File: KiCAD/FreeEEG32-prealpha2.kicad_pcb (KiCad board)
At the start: 2 copper layers, 99.1 x 99.1 mm, 205 parts, among them J1 Conn_02x08_Odd_Even, J10 Conn_02x08_Odd_Even, J11 Conn_02x08_Odd_Even, J12 Conn_02x08_Odd_Even, J13 Conn_02x08_Odd_Even, J14 Conn_02x08_Odd_Even, J15 Conn_02x08_Odd_Even, J16 Conn_02x08_Odd_Even, J17 Conn_01x03, J18 Conn_01x03, J19 Conn_01x03, J2 Conn_02x08_Odd_Even, J20 Conn_01x03, J21 Conn_01x04, J22 Conn_01x04, J23 Conn_01x02, J24 Conn_01x02, J25 Conn_02x18_Odd_Even, J26 Conn_02x18_Odd_Even, J27 Conn_02x18_Odd_Even, J28 Conn_02x18_Odd_Even, J29 Conn_01x03, J3 Conn_02x08_Odd_Even, J30 Conn_01x03, J31 Conn_01x04, J32 Conn_01x03, J33 Conn_01x03, J34 Conn_01x04, J35 Conn_01x02, J36 Conn_01x02, J37 Conn_01x05, J38 Conn_01x04, J39 Conn_02x04_Odd_Even, J4 Conn_02x08_Odd_Even, J40 Conn_02x04_Odd_Even, J41 Conn_02x04_Odd_Even, J42 Conn_02x04_Odd_Even, J43 Conn_02x04_Odd_Even, J44 Conn_02x04_Odd_Even, J5 Conn_02x08_Odd_Even, J6 Conn_02x08_Odd_Even, J7 Conn_02x08_Odd_Even, J8 Conn_02x08_Odd_Even, J9 Conn_02x08_Odd_Even, T1 da2303, U1 AD7779, U10 LP5907, U11 LSM6DS3, U12 SN6505A, U13 473521001, U14 ISO7341c, U15 ISO7341c, U16 ISO7341c, U2 AD7779, U3 AD7779, U4 AD7779, U5 LP5907, U6 LP5907, U7 ADR4525, U8 FXO-SM7_OSC-SMD7050_short, U9 STM32F765ZITx

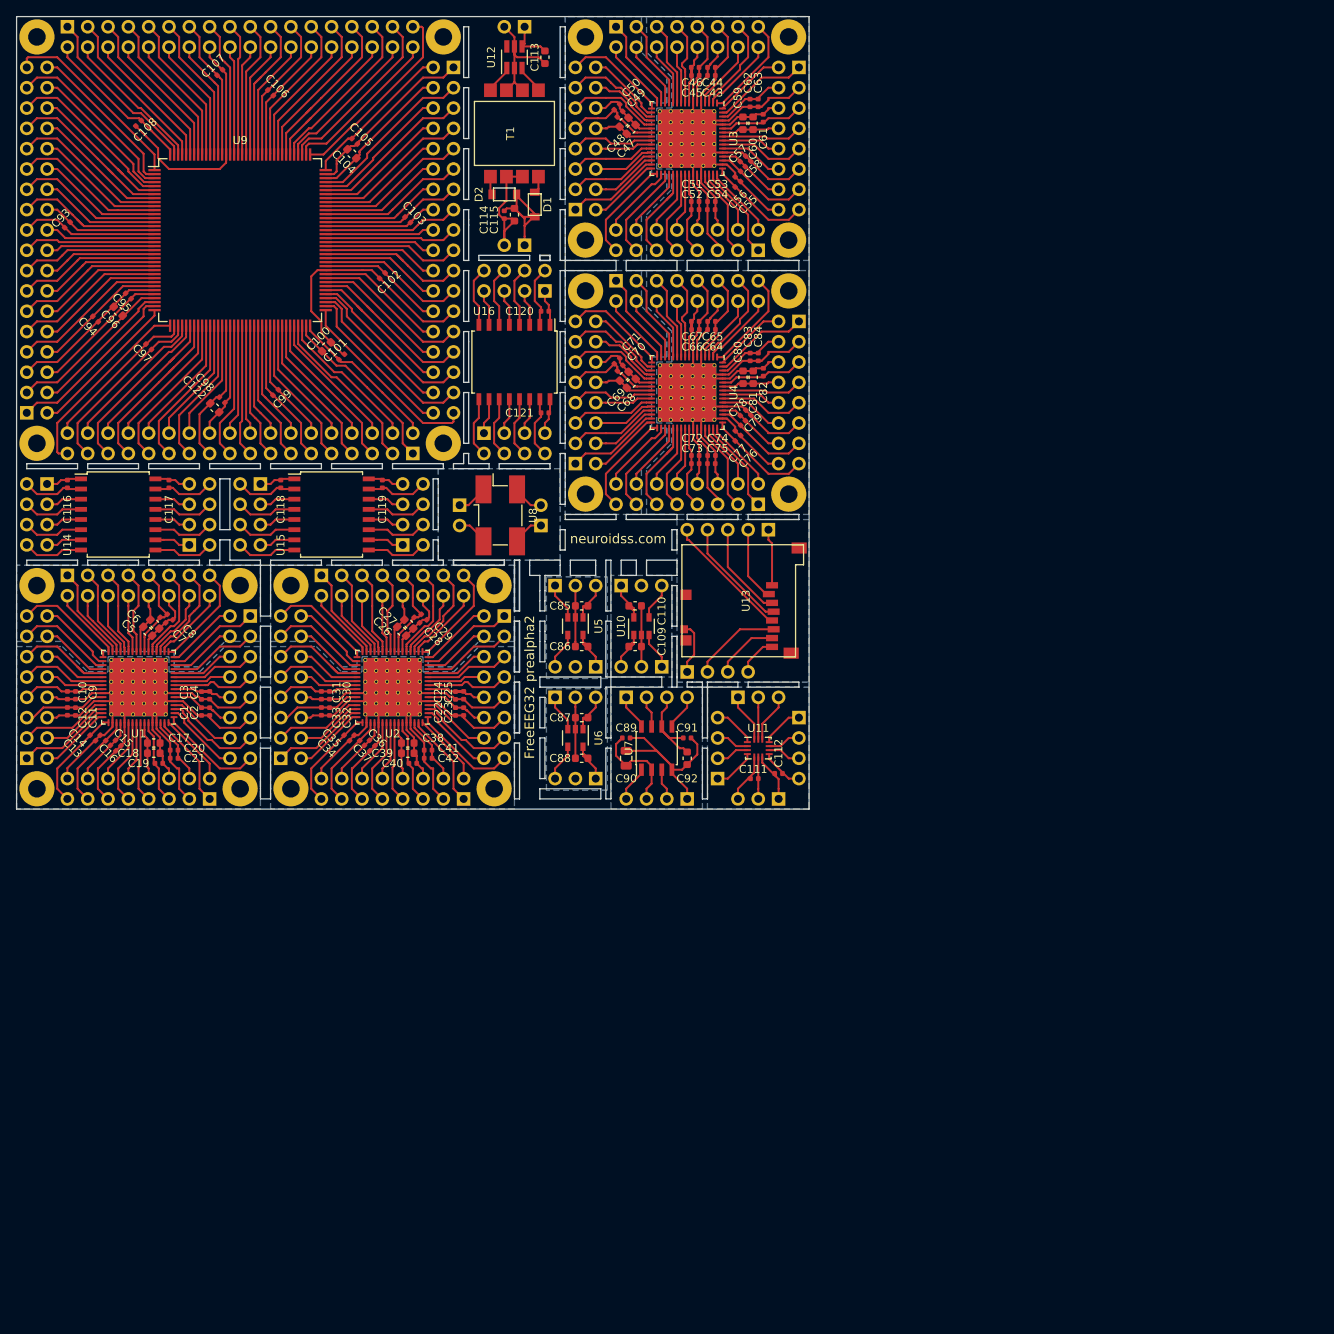
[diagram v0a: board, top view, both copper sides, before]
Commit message: added usb, crystals
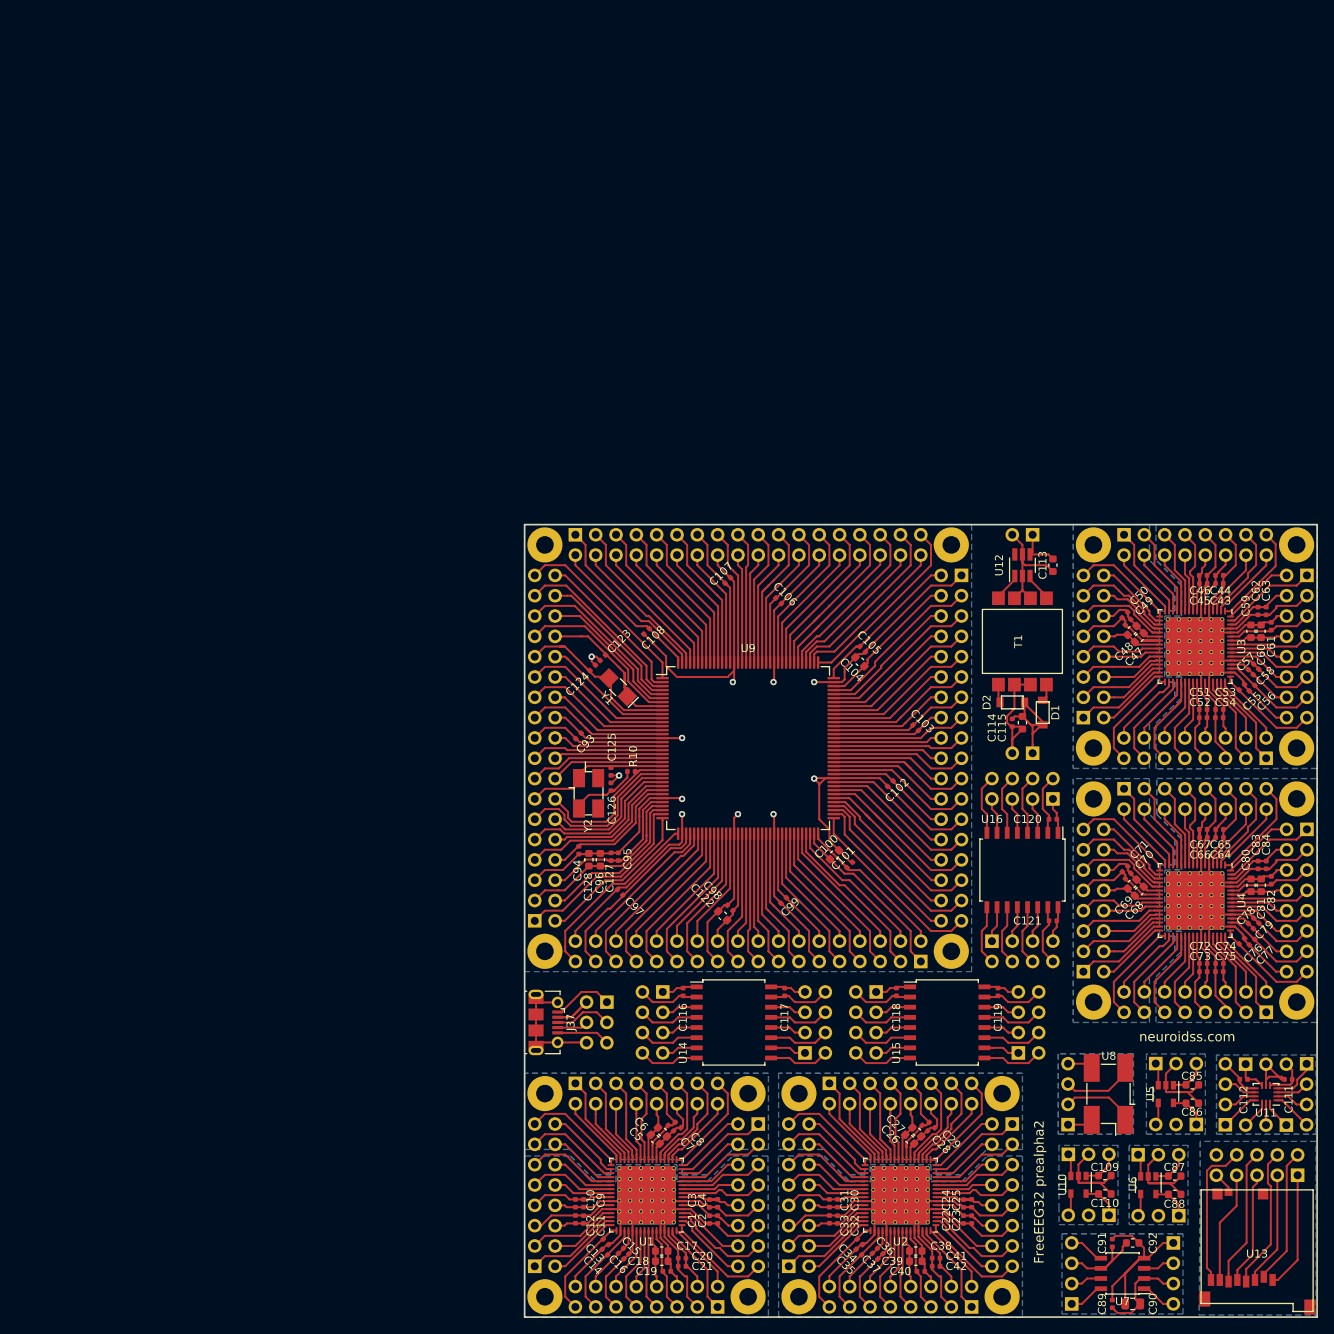
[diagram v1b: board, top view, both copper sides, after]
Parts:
- added C123: CL1, Capacitor_SMD:C_0402_1005Metric, F.Cu at (23.7, 30.6)
- added C124: CL2, Capacitor_SMD:C_0402_1005Metric, F.Cu at (22.5, 31.9)
- added C125: CL1, Capacitor_SMD:C_0402_1005Metric, F.Cu at (24.8, 44.8)
- added C126: CL2, Capacitor_SMD:C_0402_1005Metric, F.Cu at (24.8, 46.7)
- added C127: 1u, Capacitor_SMD:C_0402_1005Metric, F.Cu at (24.8, 55.5)
- added C128: 1u, Capacitor_SMD:C_0603_1608Metric, F.Cu at (22.0, 55.9)
- added R10: R_EXT, Resistor_SMD:R_0402_1005Metric, F.Cu at (27.3, 44.8)
- added Y1: 32768Hz, Crystal:Crystal_SMD_EuroQuartz_EQ161-2Pin_3.2x1.5mm_HandSoldering, F.Cu at (25.7, 34.3)
- added Y2: 8MHz, smd5032:Crystal_SMD_EuroQuartz_MJ-4Pin_5.0x3.2mm_HandSoldering, F.Cu at (22.0, 47.6)
- J23: value Conn_01x02 -> Conn_01x04; footprint Connector_PinHeader_2.54mm:PinHeader_1x02_P2.54mm_Vertical -> Connector_PinHeader_2.54mm:PinHeader_1x04_P2.54mm_Vertical
- J24: value Conn_01x02 -> Conn_02x05_Odd_Even; footprint Connector_PinHeader_2.54mm:PinHeader_1x02_P2.54mm_Vertical -> Connector_PinHeader_2.54mm:PinHeader_2x05_P2.54mm_Vertical
- J37: value Conn_01x05 -> USB_B_Micro; footprint Connector_PinHeader_2.54mm:PinHeader_1x05_P2.54mm_Vertical -> Connector_USB:USB_Micro-B_Molex-105017-0001; moved to F.Cu
- J38: value Conn_01x04 -> Conn_02x03_Odd_Even; footprint Connector_PinHeader_2.54mm:PinHeader_1x04_P2.54mm_Vertical -> Connector_PinHeader_2.54mm:PinHeader_2x03_P2.54mm_Vertical
- REF** (x20): value MountingHole_2.2mm_M2_Pad -> MH_2.2mm_M2
- moved J24 134.1 mm to (110.6, 95.3), turned to 90 degrees
- moved U8 104.9 mm to (87.0, 85.1), turned to 90 degrees
- moved U13 103.5 mm to (105.5, 104.1), turned to 0 degrees
- moved C117 99.8 mm to (46.5, 72.4)
- moved C118 99.8 mm to (60.5, 72.4)
- moved C119 99.8 mm to (73.2, 72.4)
- moved J39 99.8 mm to (31.2, 72.4)
- moved J40 99.8 mm to (49.0, 80.0)
- moved J41 99.8 mm to (57.9, 72.4)
- moved U15 99.8 mm to (66.8, 76.2)
- moved C116 99.8 mm to (33.8, 72.4)
- moved J42 99.8 mm to (75.7, 80.0)
- moved U14 99.8 mm to (40.1, 76.2)
- moved J23 99.8 mm to (81.9, 89.0)
- moved J30 99.6 mm to (87.0, 100.3), turned to 90 degrees
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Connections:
- net /ACCEL&GYRO/1 renamed /ACCEL&GYRO/1_SDO/SA0
- net /ACCEL&GYRO/10 renamed /ACCEL&GYRO/10_NC
- net /ACCEL&GYRO/11 renamed /ACCEL&GYRO/11_NC
- net /ACCEL&GYRO/12 renamed /ACCEL&GYRO/12_CS
- net /ACCEL&GYRO/13 renamed /ACCEL&GYRO/13_SCL
- net /ACCEL&GYRO/14 renamed /ACCEL&GYRO/14_SDA
- net /ACCEL&GYRO/2 renamed /ACCEL&GYRO/2_SDx
- net /ACCEL&GYRO/3 renamed /ACCEL&GYRO/3_SCx
- net /ACCEL&GYRO/4 renamed /ACCEL&GYRO/4_INT1
- net /ACCEL&GYRO/5 renamed /ACCEL&GYRO/5_VDDIO
- net /ACCEL&GYRO/6 renamed /ACCEL&GYRO/6_GND
- net /ACCEL&GYRO/7 renamed /ACCEL&GYRO/7_GND
- net /ACCEL&GYRO/8 renamed /ACCEL&GYRO/8_VDD
- net /ACCEL&GYRO/9 renamed /ACCEL&GYRO/9_INT2
- net /ADC1/1 renamed /ADC1/1_AIN0-
- net /ADC1/10 renamed /ADC1/10_AIN2+
- net /ADC1/11 renamed /ADC1/11_AIN3-
- net /ADC1/12 renamed /ADC1/12_AIN3+
- net /ADC1/13 renamed /ADC1/13_MODE0_GPIO0
- net /ADC1/14 renamed /ADC1/14_MODE1_GPIO1
- net /ADC1/15 renamed /ADC1/15_MODE2_GPIO2
- net /ADC1/16 renamed /ADC1/16_MODE3_ALERT
- net /ADC1/17 renamed /ADC1_17_CONVST_SAR
- net /ADC1/18 renamed /ADC1_18_ALERT_CS
- net /ADC1/19 renamed /ADC1_19_DCLK2_SCLK
- net /ADC1/2 renamed /ADC1/2_AIN0+
- net /ADC1/20 renamed /ADC1_20_DCLK1_SDI
- net /ADC1/21 renamed /ADC1_21_DCLK0_SDO
- net /ADC1/23 renamed /ADC1_23_DREGCAP
- net /ADC1/24 renamed /ADC1_24_IOVDD
- net /ADC1/25 renamed /ADC1_25_DOUT3
- net /ADC1/26 renamed /ADC1_26_DOUT2
- net /ADC1/27 renamed /ADC1_27_DOUT1
- net /ADC1/28 renamed /ADC1_28_DOUT0
- net /ADC1/29 renamed /ADC1_29_DCLK
- net /ADC1/3 renamed /ADC1/3_AIN1-
- net /ADC1/30 renamed /ADC1_30_DRDY
- net /ADC1/31 renamed /ADC1_31_XTAL1
- net /ADC1/32 renamed /ADC1_32_XTAL2_MCLK
- net /ADC1/33 renamed /ADC1_33_START
- net /ADC1/34 renamed /ADC1_34_SYNC_OUT
- net /ADC1/35 renamed /ADC1_35_SYNC_IN
- net /ADC1/36 renamed /ADC1_36_RESET
- net /ADC1/37 renamed /ADC1/37_AIN7+
- net /ADC1/38 renamed /ADC1/38_AIN7-
- net /ADC1/39 renamed /ADC1/39_AIN6+
- net /ADC1/4 renamed /ADC1/4_AIN1+
- net /ADC1/40 renamed /ADC1/40_AIN6-
- net /ADC1/41 renamed /ADC1_41_REF2+
- net /ADC1/43 renamed /ADC1_43_AVDD1B
- net /ADC1/45 renamed /ADC1/45_AIN5+
- net /ADC1/46 renamed /ADC1/46_AIN5-
- net /ADC1/47 renamed /ADC1/47_AIN4+
- net /ADC1/48 renamed /ADC1/48_AIN4-
- net /ADC1/49 renamed /ADC1/49_REF_OUT
- net /ADC1/51 renamed /ADC1/51_AREG2CAP
- net /ADC1/52 renamed /ADC1_52_AVDD2B
- net /ADC1/54 renamed /ADC1_54_FORMAT1
- net /ADC1/55 renamed /ADC1_55_FORMAT0
- net /ADC1/56 renamed /ADC1_56_CLK_SEL
- net /ADC1/57 renamed /ADC1/57_VCM
- net /ADC1/58 renamed /ADC1_58_AVDD2A
- net /ADC1/59 renamed /ADC1/59_AREG1CAP
- net /ADC1/6 renamed /ADC1_6_AVDD1A
- net /ADC1/62 renamed /ADC1_62_AVDD4
- net /ADC1/63 renamed /ADC1/63_AUXAIN+
- net /ADC1/64 renamed /ADC1/64_AUXAIN-
- net /ADC1/8 renamed /ADC1_8_REF1+
- net /ADC1/9 renamed /ADC1/9_AIN2-
- net /ADC2/1 renamed /ADC2/1_AIN0-
- net /ADC2/10 renamed /ADC2/10_AIN2+
- net /ADC2/11 renamed /ADC2/11_AIN3-
- net /ADC2/12 renamed /ADC2/12_AIN3+
- net /ADC2/13 renamed /ADC2/13_MODE0_GPIO0
- net /ADC2/14 renamed /ADC2/14_MODE1_GPIO1
- net /ADC2/15 renamed /ADC2/15_MODE2_GPIO2
- net /ADC2/16 renamed /ADC2/16_MODE3_ALERT
- net /ADC2/17 renamed /ADC2_17_CONVST_SAR
- net /ADC2/18 renamed /ADC2_18_ALERT_CS
- net /ADC2/19 renamed /ADC2_19_DCLK2_SCLK
- net /ADC2/2 renamed /ADC2/2_AIN0+
- net /ADC2/20 renamed /ADC2_20_DCLK1_SDI
- net /ADC2/21 renamed /ADC2_21_DCLK0_SDO
- net /ADC2/23 renamed /ADC2_23_DREGCAP
- net /ADC2/24 renamed /ADC2_24_IOVDD
- net /ADC2/25 renamed /ADC2_25_DOUT3
- net /ADC2/26 renamed /ADC2_26_DOUT2
- net /ADC2/27 renamed /ADC2_27_DOUT1
- net /ADC2/28 renamed /ADC2_28_DOUT0
- net /ADC2/29 renamed /ADC2_29_DCLK
- net /ADC2/3 renamed /ADC2/3_AIN1-
- net /ADC2/30 renamed /ADC2_30_DRDY
- net /ADC2/31 renamed /ADC2_31_XTAL1
- net /ADC2/32 renamed /ADC2_32_XTAL2_MCLK
- net /ADC2/33 renamed /ADC2_33_START
- net /ADC2/34 renamed /ADC2_34_SYNC_OUT
- net /ADC2/35 renamed /ADC2_35_SYNC_IN
- net /ADC2/36 renamed /ADC2_36_RESET
- net /ADC2/37 renamed /ADC2/37_AIN7+
- net /ADC2/38 renamed /ADC2/38_AIN7-
- net /ADC2/39 renamed /ADC2/39_AIN6+
- net /ADC2/4 renamed /ADC2/4_AIN1+
- net /ADC2/40 renamed /ADC2/40_AIN6-
- net /ADC2/41 renamed /ADC2_41_REF2+
- net /ADC2/43 renamed /ADC2_43_AVDD1B
- net /ADC2/45 renamed /ADC2/45_AIN5+
- net /ADC2/46 renamed /ADC2/46_AIN5-
- net /ADC2/47 renamed /ADC2/47_AIN4+
- net /ADC2/48 renamed /ADC2/48_AIN4-
- net /ADC2/49 renamed /ADC2/49_REF_OUT
- net /ADC2/51 renamed /ADC2/51_AREG2CAP
- net /ADC2/52 renamed /ADC2_52_AVDD2B
- net /ADC2/54 renamed /ADC2_54_FORMAT1
- net /ADC2/55 renamed /ADC2_55_FORMAT0
- net /ADC2/56 renamed /ADC2_56_CLK_SEL
- net /ADC2/57 renamed /ADC2/57_VCM
- net /ADC2/58 renamed /ADC2_58_AVDD2A
- net /ADC2/59 renamed /ADC2/59_AREG1CAP
- net /ADC2/6 renamed /ADC2_6_AVDD1A
- net /ADC2/62 renamed /ADC2_62_AVDD4
- net /ADC2/63 renamed /ADC2/63_AUXAIN+
- net /ADC2/64 renamed /ADC2/64_AUXAIN-
- net /ADC2/8 renamed /ADC2_8_REF1+
- net /ADC2/9 renamed /ADC2/9_AIN2-
- net /ADC3/1 renamed /ADC3/1_AIN0-
- net /ADC3/10 renamed /ADC3/10_AIN2+
- net /ADC3/11 renamed /ADC3/11_AIN3-
- net /ADC3/12 renamed /ADC3/12_AIN3+
- net /ADC3/13 renamed /ADC3/13_MODE0_GPIO0
- net /ADC3/14 renamed /ADC3/14_MODE1_GPIO1
- net /ADC3/15 renamed /ADC3/15_MODE2_GPIO2
- net /ADC3/16 renamed /ADC3/16_MODE3_ALERT
- net /ADC3/17 renamed /ADC3_17_CONVST_SAR
- net /ADC3/18 renamed /ADC3_18_ALERT_CS
- net /ADC3/19 renamed /ADC3_19_DCLK2_SCLK
- net /ADC3/2 renamed /ADC3/2_AIN0+
- net /ADC3/20 renamed /ADC3_20_DCLK1_SDI
- net /ADC3/21 renamed /ADC3_21_DCLK0_SDO
- net /ADC3/23 renamed /ADC3_23_DREGCAP
- net /ADC3/24 renamed /ADC3_24_IOVDD
- net /ADC3/25 renamed /ADC3_25_DOUT3
- net /ADC3/26 renamed /ADC3_26_DOUT2
- net /ADC3/27 renamed /ADC3_27_DOUT1
- net /ADC3/28 renamed /ADC3_28_DOUT0
- net /ADC3/29 renamed /ADC3_29_DCLK
- net /ADC3/3 renamed /ADC3/3_AIN1-
- net /ADC3/30 renamed /ADC3_30_DRDY
- net /ADC3/31 renamed /ADC3_31_XTAL1
- net /ADC3/32 renamed /ADC3_32_XTAL2_MCLK
- net /ADC3/33 renamed /ADC3_33_START
- net /ADC3/34 renamed /ADC3_34_SYNC_OUT
- net /ADC3/35 renamed /ADC3_35_SYNC_IN
- net /ADC3/36 renamed /ADC3_36_RESET
- net /ADC3/37 renamed /ADC3/37_AIN7+
- net /ADC3/38 renamed /ADC3/38_AIN7-
- net /ADC3/39 renamed /ADC3/39_AIN6+
- net /ADC3/4 renamed /ADC3/4_AIN1+
- net /ADC3/40 renamed /ADC3/40_AIN6-
- net /ADC3/41 renamed /ADC3_41_REF2+
- net /ADC3/43 renamed /ADC3_43_AVDD1B
- net /ADC3/45 renamed /ADC3/45_AIN5+
- net /ADC3/46 renamed /ADC3/46_AIN5-
- net /ADC3/47 renamed /ADC3/47_AIN4+
- net /ADC3/48 renamed /ADC3/48_AIN4-
- net /ADC3/49 renamed /ADC3/49_REF_OUT
- net /ADC3/51 renamed /ADC3/51_AREG2CAP
- net /ADC3/52 renamed /ADC3_52_AVDD2B
- net /ADC3/54 renamed /ADC3_54_FORMAT1
- net /ADC3/55 renamed /ADC3_55_FORMAT0
- net /ADC3/56 renamed /ADC3_56_CLK_SEL
- net /ADC3/57 renamed /ADC3/57_VCM
- net /ADC3/58 renamed /ADC3_58_AVDD2A
- net /ADC3/59 renamed /ADC3/59_AREG1CAP
- net /ADC3/6 renamed /ADC3_6_AVDD1A
- net /ADC3/62 renamed /ADC3_62_AVDD4
- net /ADC3/63 renamed /ADC3/63_AUXAIN+
- net /ADC3/64 renamed /ADC3/64_AUXAIN-
- net /ADC3/8 renamed /ADC3_8_REF1+
- net /ADC3/9 renamed /ADC3/9_AIN2-
- net /ADC4/1 renamed /ADC4/1_AIN0-
- net /ADC4/10 renamed /ADC4/10_AIN2+
- net /ADC4/11 renamed /ADC4/11_AIN3-
- net /ADC4/12 renamed /ADC4/12_AIN3+
- net /ADC4/13 renamed /ADC4/13_MODE0_GPIO0
- net /ADC4/14 renamed /ADC4/14_MODE1_GPIO1
- net /ADC4/15 renamed /ADC4/15_MODE2_GPIO2
- net /ADC4/16 renamed /ADC4/16_MODE3_ALERT
- net /ADC4/17 renamed /ADC4_17_CONVST_SAR
- net /ADC4/18 renamed /ADC4_18_ALERT_CS
- net /ADC4/19 renamed /ADC4_19_DCLK2_SCLK
- net /ADC4/2 renamed /ADC4/2_AIN0+
- net /ADC4/20 renamed /ADC4_20_DCLK1_SDI
- net /ADC4/21 renamed /ADC4_21_DCLK0_SDO
- net /ADC4/23 renamed /ADC4_23_DREGCAP
- net /ADC4/24 renamed /ADC4_24_IOVDD
- net /ADC4/25 renamed /ADC4_25_DOUT3
- net /ADC4/26 renamed /ADC4_26_DOUT2
- net /ADC4/27 renamed /ADC4_27_DOUT1
- net /ADC4/28 renamed /ADC4_28_DOUT0
- net /ADC4/29 renamed /ADC4_29_DCLK
- net /ADC4/3 renamed /ADC4/3_AIN1-
- net /ADC4/30 renamed /ADC4_30_DRDY
- net /ADC4/31 renamed /ADC4_31_XTAL1
- net /ADC4/32 renamed /ADC4_32_XTAL2_MCLK
- net /ADC4/33 renamed /ADC4_33_START
- net /ADC4/34 renamed /ADC4_34_SYNC_OUT
- net /ADC4/35 renamed /ADC4_35_SYNC_IN
- net /ADC4/36 renamed /ADC4_36_RESET
- net /ADC4/37 renamed /ADC4/37_AIN7+
- net /ADC4/38 renamed /ADC4/38_AIN7-
- net /ADC4/39 renamed /ADC4/39_AIN6+
- net /ADC4/4 renamed /ADC4/4_AIN1+
- net /ADC4/40 renamed /ADC4/40_AIN6-
- net /ADC4/41 renamed /ADC4_41_REF2+
- net /ADC4/43 renamed /ADC4_43_AVDD1B
- net /ADC4/45 renamed /ADC4/45_AIN5+
- net /ADC4/46 renamed /ADC4/46_AIN5-
- net /ADC4/47 renamed /ADC4/47_AIN4+
- net /ADC4/48 renamed /ADC4/48_AIN4-
- net /ADC4/49 renamed /ADC4/49_REF_OUT
- net /ADC4/51 renamed /ADC4/51_AREG2CAP
- net /ADC4/52 renamed /ADC4_52_AVDD2B
- net /ADC4/54 renamed /ADC4_54_FORMAT1
- net /ADC4/55 renamed /ADC4_55_FORMAT0
- net /ADC4/56 renamed /ADC4_56_CLK_SEL
- net /ADC4/57 renamed /ADC4/57_VCM
- net /ADC4/58 renamed /ADC4_58_AVDD2A
- net /ADC4/59 renamed /ADC4/59_AREG1CAP
- net /ADC4/6 renamed /ADC4_6_AVDD1A
- net /ADC4/62 renamed /ADC4_62_AVDD4
- net /ADC4/63 renamed /ADC4/63_AUXAIN+
- net /ADC4/64 renamed /ADC4/64_AUXAIN-
- net /ADC4/8 renamed /ADC4_8_REF1+
- net /ADC4/9 renamed /ADC4/9_AIN2-
- net /AVDD/1 renamed /VDD_1_IN
- net /AVDD/2 renamed /VDD_2_GND
- net /AVDD/3 renamed /VDD_3_EN
- net /AVDD/4 renamed /VDD/4_NC
- net /AVDD/5 renamed /VDD_5_OUT
- net /IOVDD/1 renamed /IOVDD_1_IN
- net /IOVDD/2 renamed /IOVDD_2_GND
- net /IOVDD/3 renamed /IOVDD_3_EN
- net /IOVDD/4 renamed /IOVDD/4_NC
- net /IOVDD/5 renamed /IOVDD_5_OUT
- net /ISO1/1 renamed /ISO1/1_VCC1
- net /ISO1/10 renamed /ISO1/10_EN2
- net /ISO1/11 renamed /ISO1/11_IND
- net /ISO1/12 renamed /ISO1/12_OUTC
- net /ISO1/13 renamed /ISO1/13_OUTB
- net /ISO1/14 renamed /ISO1/14_OUTA
- net /ISO1/15 renamed /ISO1/15_GND2
- net /ISO1/16 renamed /ISO1/16_VCC2
- net /ISO1/2 renamed /ISO1/2_GND1
- net /ISO1/3 renamed /ISO1/3_INA
- net /ISO1/4 renamed /ISO1/4_INB
- net /ISO1/5 renamed /ISO1/5_INC
- net /ISO1/6 renamed /ISO1/6_OUTD
- net /ISO1/7 renamed /ISO1/7_EN1
- net /ISO1/8 renamed /ISO1/8_GND1
- net /ISO1/9 renamed /ISO1/9_GND2
- net /ISO2/1 renamed /ISO2/1_VCC1
- net /ISO2/10 renamed /ISO2/10_EN2
- net /ISO2/11 renamed /ISO2/11_IND
- net /ISO2/12 renamed /ISO2/12_OUTC
- net /ISO2/13 renamed /ISO2/13_OUTB
- net /ISO2/14 renamed /ISO2/14_OUTA
- net /ISO2/15 renamed /ISO2/15_GND2
- net /ISO2/16 renamed /ISO2/16_VCC2
- net /ISO2/2 renamed /ISO2/2_GND1
- net /ISO2/3 renamed /ISO2/3_INA
- net /ISO2/4 renamed /ISO2/4_INB
- net /ISO2/5 renamed /ISO2/5_INC
- net /ISO2/6 renamed /ISO2/6_OUTD
- net /ISO2/7 renamed /ISO2/7_EN1
- net /ISO2/8 renamed /ISO2/8_GND1
- net /ISO2/9 renamed /ISO2/9_GND2
- net /ISO3/1 renamed /ISO3/1_VCC1
- net /ISO3/10 renamed /ISO3/10_EN2
- net /ISO3/11 renamed /ISO3/11_IND
- net /ISO3/12 renamed /ISO3/12_OUTC
- net /ISO3/13 renamed /ISO3/13_OUTB
- net /ISO3/14 renamed /ISO3/14_OUTA
- net /ISO3/15 renamed /ISO3/15_GND2
- net /ISO3/16 renamed /ISO3/16_VCC2
- net /ISO3/2 renamed /ISO3/2_GND1
- net /ISO3/3 renamed /ISO3/3_INA
- net /ISO3/4 renamed /ISO3/4_INB
- net /ISO3/5 renamed /ISO3/5_INC
- net /ISO3/6 renamed /ISO3/6_OUTD
- net /ISO3/7 renamed /ISO3/7_EN1
- net /ISO3/8 renamed /ISO3/8_GND1
- net /ISO3/9 renamed /ISO3/9_GND2
- net /MCU/1 renamed /MCU/1_PE2
- net /MCU/10 renamed /MCU/10_PF0
- net /MCU/100 renamed /MCU/100_PA8
- net /MCU/101 renamed /MCU/101_PA9
- net /MCU/102 renamed /MCU/102_PA10
- net /MCU/103 renamed /MCU_103_PA11_USB_OTG_FS_DM
- net /MCU/104 renamed /MCU_104_PA12_USB_OTG_FS_DP
- net /MCU/105 renamed /MCU/105_PA13
- net /MCU/106 renamed /MCU/106_VCAP_2
- net /MCU/108 renamed /MCU_108_VDD
- net /MCU/109 renamed /MCU/109_PA14
- net /MCU/11 renamed /MCU/11_PF1
- net /MCU/110 renamed /MCU/110_PA15
- net /MCU/111 renamed /MCU/111_PC10
- net /MCU/112 renamed /MCU/112_PC11
- net /MCU/113 renamed /MCU/113_PC12
- net /MCU/114 renamed /MCU/114_PD0
- net /MCU/115 renamed /MCU/115_PD1
- net /MCU/116 renamed /MCU/116_PD2
- net /MCU/117 renamed /MCU/117_PD3
- net /MCU/118 renamed /MCU/118_PD4
- net /MCU/119 renamed /MCU/119_PD5
- net /MCU/12 renamed /MCU/12_PF2
- net /MCU/121 renamed /MCU_121_VDDSDMMC
- net /MCU/122 renamed /MCU/122_PD6
- net /MCU/123 renamed /MCU/123_PD7
- net /MCU/124 renamed /MCU/124_PG9
- net /MCU/125 renamed /MCU/125_PG10
- net /MCU/126 renamed /MCU/126_PG11
- net /MCU/127 renamed /MCU/127_PG12
- net /MCU/128 renamed /MCU/128_PG13
- net /MCU/129 renamed /MCU/129_PG14
- net /MCU/13 renamed /MCU/13_PF3
- net /MCU/131 renamed /MCU_131_VDD
- net /MCU/132 renamed /MCU/132_PG15
- net /MCU/133 renamed /MCU/133_PB3
- net /MCU/134 renamed /MCU/134_PB4
- net /MCU/135 renamed /MCU/135_PB5
- net /MCU/136 renamed /MCU/136_PB6
- net /MCU/137 renamed /MCU/137_PB7
- net /MCU/138 renamed /MCU/138_BOOT0
- net /MCU/139 renamed /MCU/139_PB8
- net /MCU/14 renamed /MCU/14_PF4
- net /MCU/140 renamed /MCU/140_PB9
- net /MCU/141 renamed /MCU/141_PE0
- net /MCU/142 renamed /MCU/142_PE1
- net /MCU/143 renamed /MCU/143_PDR_ON
- net /MCU/144 renamed /MCU_144_VDD
- net /MCU/15 renamed /MCU/15_PF5
- net /MCU/17 renamed /MCU_17_VDD
- net /MCU/18 renamed /MCU/18_PF6
- net /MCU/19 renamed /MCU/19_PF7
- net /MCU/2 renamed /MCU/2_PE3
- net /MCU/20 renamed /MCU/20_PF8
- net /MCU/21 renamed /MCU/21_PF9
- net /MCU/22 renamed /MCU/22_PF10
- net /MCU/23 renamed /MCU/23_PH0
- net /MCU/24 renamed /MCU/24_PH1
- net /MCU/25 renamed /MCU/25_NRST
- net /MCU/26 renamed /MCU/26_PC0
- net /MCU/27 renamed /MCU/27_PC1
- net /MCU/28 renamed /MCU/28_PC2
- net /MCU/29 renamed /MCU/29_PC3
- net /MCU/3 renamed /MCU/3_PE4
- net /MCU/30 renamed /MCU_30_VDD
- net /MCU/32 renamed /MCU/32_VREF+
- net /MCU/33 renamed /MCU_33_VDDA
- net /MCU/34 renamed /MCU/34_PA0
- net /MCU/35 renamed /MCU/35_PA1
- net /MCU/36 renamed /MCU/36_PA2
- net /MCU/37 renamed /MCU/37_PA3
- net /MCU/39 renamed /MCU_39_VDD
- net /MCU/4 renamed /MCU/4_PE5
- net /MCU/40 renamed /MCU/40_PA4
- net /MCU/41 renamed /MCU/41_PA5
- net /MCU/42 renamed /MCU/42_PA6
- net /MCU/43 renamed /MCU/43_PA7
- net /MCU/44 renamed /MCU/44_PC4
- net /MCU/45 renamed /MCU/45_PC5
- net /MCU/46 renamed /MCU/46_PB0
- net /MCU/47 renamed /MCU/47_PB1
- net /MCU/48 renamed /MCU/48_PB2
- net /MCU/49 renamed /MCU/49_PF11
- net /MCU/5 renamed /MCU/5_PE6
- net /MCU/50 renamed /MCU/50_PF12
- net /MCU/52 renamed /MCU_52_VDD
- net /MCU/53 renamed /MCU/53_PF13
- net /MCU/54 renamed /MCU/54_PF14
- net /MCU/55 renamed /MCU/55_PF15
- net /MCU/56 renamed /MCU/56_PG0
- net /MCU/57 renamed /MCU/57_PG1
- net /MCU/58 renamed /MCU/58_PE7
- net /MCU/59 renamed /MCU/59_PE8
- net /MCU/6 renamed /MCU/6_VBAT
- net /MCU/60 renamed /MCU/60_PE9
- net /MCU/62 renamed /MCU_62_VDD
- net /MCU/63 renamed /MCU/63_PE10
- net /MCU/64 renamed /MCU/64_PE11
- net /MCU/65 renamed /MCU/65_PE12
- net /MCU/66 renamed /MCU/66_PE13
- net /MCU/67 renamed /MCU/67_PE14
- net /MCU/68 renamed /MCU/68_PE15
- net /MCU/69 renamed /MCU/69_PB10
- net /MCU/7 renamed /MCU/7_PC13
- net /MCU/70 renamed /MCU/70_PB11
- net /MCU/71 renamed /MCU/71_VCAP_1
- net /MCU/72 renamed /MCU_72_VDD
- net /MCU/73 renamed /MCU/73_PB12
- net /MCU/74 renamed /MCU/74_PB13
- net /MCU/75 renamed /MCU/75_PB14
- net /MCU/76 renamed /MCU/76_PB15
- net /MCU/77 renamed /MCU/77_PD8
- net /MCU/78 renamed /MCU/78_PD9
- net /MCU/79 renamed /MCU/79_PD10
- net /MCU/8 renamed /MCU/8_PC14
- net /MCU/80 renamed /MCU/80_PD11
- net /MCU/81 renamed /MCU/81_PD12
- net /MCU/82 renamed /MCU/82_PD13
- net /MCU/84 renamed /MCU_84_VDD
- net /MCU/85 renamed /MCU/85_PD14
- net /MCU/86 renamed /MCU/86_PD15
- net /MCU/87 renamed /MCU/87_PG2
- net /MCU/88 renamed /MCU/88_PG3
- net /MCU/89 renamed /MCU/89_PG4
- net /MCU/9 renamed /MCU/9_PC15
- net /MCU/90 renamed /MCU/90_PG5
- net /MCU/91 renamed /MCU/91_PG6
- net /MCU/92 renamed /MCU/92_PG7
- net /MCU/93 renamed /MCU/93_PG8
- net /MCU/95 renamed /MCU_95_VDDUSB
- net /MCU/96 renamed /MCU/96_PC6
- net /MCU/97 renamed /MCU/97_PC7
- net /MCU/98 renamed /MCU/98_PC8
- net /MCU/99 renamed /MCU/99_PC9
- net /POWER/1 renamed /POWER/1_GND
- net /POWER/2 renamed /POWER/2_VCC
- net /POWER/3 renamed /POWER_3_OUT1A2B_DIODES
- net /POWER/4 renamed /POWER_4_OUT1B2A
- net /REF/1 renamed /REF/1_NC
- net /REF/2 renamed /REF_2_VIN
- net /REF/3 renamed /REF/3_NC
- net /REF/4 renamed /REF_4_GND
- net /REF/5 renamed /REF/5_NC
- net /REF/6 renamed /REF_6_OUT
- net /REF/7 renamed /REF/7_NC
- net /REF/8 renamed /REF/8_TP
- net /VDD/1 renamed /AVDD_1_IN
- net /VDD/2 renamed /AVDD_2_GND
- net /VDD/3 renamed /AVDD_3_EN
- net /VDD/4 renamed /AVDD/4_NC
- net /VDD/5 renamed /AVDD_5_OUT
- net VSS renamed /MCU_107_VSS
- C1 pad 1: AVSS -> /ADC1_42_REF2-
- C10 pad 1: AVSS -> /ADC1_42_REF2-
- C11 pad 1: AVSS -> /ADC1_42_REF2-
- C12 pad 1: AVSS -> /ADC1_42_REF2-
- C13 pad 2: AVSS -> /ADC1_42_REF2-
- C14 pad 2: AVSS -> /ADC1_42_REF2-
- C15 pad 1: AVSS -> /ADC1_42_REF2-
- C16 pad 1: AVSS -> /ADC1_42_REF2-
- C17 pad 1: AVSS -> /ADC1_42_REF2-
- C18 pad 1: AVSS -> /ADC1_42_REF2-
- C19 pad 2: AVSS -> /ADC1_42_REF2-
- C2 pad 1: AVSS -> /ADC1_42_REF2-
- C20 pad 2: AVSS -> /ADC1_42_REF2-
- C21 pad 2: AVSS -> /ADC1_42_REF2-
- C22 pad 1: AVSS -> /ADC2_42_REF2-
- C23 pad 1: AVSS -> /ADC2_42_REF2-
- C24 pad 1: AVSS -> /ADC2_42_REF2-
- C25 pad 1: AVSS -> /ADC2_42_REF2-
- C26 pad 1: DGND -> /ADC2_22_DGND
- C27 pad 1: DGND -> /ADC2_22_DGND
- C28 pad 1: DGND -> /ADC2_22_DGND
- C29 pad 1: DGND -> /ADC2_22_DGND
- C3 pad 1: AVSS -> /ADC1_42_REF2-
- C30 pad 1: AVSS -> /ADC2_42_REF2-
- C31 pad 1: AVSS -> /ADC2_42_REF2-
- C32 pad 1: AVSS -> /ADC2_42_REF2-
- C33 pad 1: AVSS -> /ADC2_42_REF2-
- C34 pad 2: AVSS -> /ADC2_42_REF2-
- C35 pad 2: AVSS -> /ADC2_42_REF2-
- C36 pad 1: AVSS -> /ADC2_42_REF2-
- C37 pad 1: AVSS -> /ADC2_42_REF2-
- C38 pad 1: AVSS -> /ADC2_42_REF2-
- C39 pad 1: AVSS -> /ADC2_42_REF2-
- C4 pad 1: AVSS -> /ADC1_42_REF2-
- C40 pad 2: AVSS -> /ADC2_42_REF2-
- C41 pad 2: AVSS -> /ADC2_42_REF2-
- C42 pad 2: AVSS -> /ADC2_42_REF2-
- C43 pad 1: AVSS -> /ADC3_42_REF2-
- C44 pad 1: AVSS -> /ADC3_42_REF2-
- C45 pad 1: AVSS -> /ADC3_42_REF2-
- C46 pad 1: AVSS -> /ADC3_42_REF2-
- C47 pad 1: DGND -> /ADC3_22_DGND
- C48 pad 1: DGND -> /ADC3_22_DGND
- C49 pad 1: DGND -> /ADC3_22_DGND
- C5 pad 1: DGND -> /ADC1_22_DGND
- C50 pad 1: DGND -> /ADC3_22_DGND
- C51 pad 1: AVSS -> /ADC3_42_REF2-
- C52 pad 1: AVSS -> /ADC3_42_REF2-
- C53 pad 1: AVSS -> /ADC3_42_REF2-
- C54 pad 1: AVSS -> /ADC3_42_REF2-
- C55 pad 2: AVSS -> /ADC3_42_REF2-
- C56 pad 2: AVSS -> /ADC3_42_REF2-
- C57 pad 1: AVSS -> /ADC3_42_REF2-
- C58 pad 1: AVSS -> /ADC3_42_REF2-
- C59 pad 1: AVSS -> /ADC3_42_REF2-
- C6 pad 1: DGND -> /ADC1_22_DGND
- C60 pad 1: AVSS -> /ADC3_42_REF2-
- C61 pad 2: AVSS -> /ADC3_42_REF2-
- C62 pad 2: AVSS -> /ADC3_42_REF2-
- C63 pad 2: AVSS -> /ADC3_42_REF2-
- C64 pad 1: AVSS -> /ADC4_42_REF2-
- C65 pad 1: AVSS -> /ADC4_42_REF2-
- C66 pad 1: AVSS -> /ADC4_42_REF2-
- C67 pad 1: AVSS -> /ADC4_42_REF2-
- C68 pad 1: DGND -> /ADC4_22_DGND
- C69 pad 1: DGND -> /ADC4_22_DGND
- C7 pad 1: DGND -> /ADC1_22_DGND
- C70 pad 1: DGND -> /ADC4_22_DGND
- C71 pad 1: DGND -> /ADC4_22_DGND
- C72 pad 1: AVSS -> /ADC4_42_REF2-
- C73 pad 1: AVSS -> /ADC4_42_REF2-
- C74 pad 1: AVSS -> /ADC4_42_REF2-
- C75 pad 1: AVSS -> /ADC4_42_REF2-
- C76 pad 2: AVSS -> /ADC4_42_REF2-
- C77 pad 2: AVSS -> /ADC4_42_REF2-
- C78 pad 1: AVSS -> /ADC4_42_REF2-
- C79 pad 1: AVSS -> /ADC4_42_REF2-
- C8 pad 1: DGND -> /ADC1_22_DGND
- C80 pad 1: AVSS -> /ADC4_42_REF2-
- C81 pad 1: AVSS -> /ADC4_42_REF2-
- C82 pad 2: AVSS -> /ADC4_42_REF2-
- C83 pad 2: AVSS -> /ADC4_42_REF2-
- C84 pad 2: AVSS -> /ADC4_42_REF2-
- C9 pad 1: AVSS -> /ADC1_42_REF2-
- J1 pad 11: AVSS -> /ADC1_42_REF2-
- J1 pad 9: AVSS -> /ADC1_42_REF2-
- J10 pad 12: DGND -> /ADC3_22_DGND
- J11 pad 6: AVSS -> /ADC3_42_REF2-
- J11 pad 8: AVSS -> /ADC3_42_REF2-
- J12 pad 11: AVSS -> /ADC3_42_REF2-
- J12 pad 16: AVSS -> /ADC3_42_REF2-
- J12 pad 3: AVSS -> /ADC3_42_REF2-
- J12 pad 6: AVSS -> /ADC3_42_REF2-
- J13 pad 11: AVSS -> /ADC4_42_REF2-
- J13 pad 9: AVSS -> /ADC4_42_REF2-
- J14 pad 12: DGND -> /ADC4_22_DGND
- J15 pad 6: AVSS -> /ADC4_42_REF2-
- J15 pad 8: AVSS -> /ADC4_42_REF2-
- J16 pad 11: AVSS -> /ADC4_42_REF2-
- J16 pad 16: AVSS -> /ADC4_42_REF2-
- J16 pad 3: AVSS -> /ADC4_42_REF2-
- J16 pad 6: AVSS -> /ADC4_42_REF2-
- J2 pad 12: DGND -> /ADC1_22_DGND
- J23 pad 1: /CRYSTAL/3 -> /CRYSTAL_4_Vin
- J23 pad 2: /CRYSTAL/4 -> /CRYSTAL/1_NC
- J24 pad 1: /CRYSTAL/1 -> /SD/1_DATA2
- J24 pad 2: /CRYSTAL/2 -> /SD/2_DATA3
- J3 pad 6: AVSS -> /ADC1_42_REF2-
- J3 pad 8: AVSS -> /ADC1_42_REF2-
- J37 pad 1: /SD/1 -> /USB_1_VBUS
- J37 pad 2: /SD/2 -> /USB_2_D-
- J37 pad 3: /SD/3 -> /USB_3_D+
- J37 pad 4: /SD/4 -> /USB/4_ID
- J37 pad 5: /SD/5 -> /USB_5_GND
- J38 pad 1: /SD/9 -> /USB_1_VBUS
- J38 pad 2: /SD/6 -> /USB_2_D-
- J38 pad 3: /SD/7 -> /USB_3_D+
- J38 pad 4: /SD/8 -> /USB/4_ID
- J4 pad 11: AVSS -> /ADC1_42_REF2-
- J4 pad 16: AVSS -> /ADC1_42_REF2-
- J4 pad 3: AVSS -> /ADC1_42_REF2-
- J4 pad 6: AVSS -> /ADC1_42_REF2-
- J5 pad 11: AVSS -> /ADC2_42_REF2-
- J5 pad 9: AVSS -> /ADC2_42_REF2-
- J6 pad 12: DGND -> /ADC2_22_DGND
- J7 pad 6: AVSS -> /ADC2_42_REF2-
- J7 pad 8: AVSS -> /ADC2_42_REF2-
- J8 pad 11: AVSS -> /ADC2_42_REF2-
- J8 pad 16: AVSS -> /ADC2_42_REF2-
- J8 pad 3: AVSS -> /ADC2_42_REF2-
- J8 pad 6: AVSS -> /ADC2_42_REF2-
- J9 pad 11: AVSS -> /ADC3_42_REF2-
- J9 pad 9: AVSS -> /ADC3_42_REF2-
- U1 pad 22: DGND -> /ADC1_22_DGND
- U1 pad 42: AVSS -> /ADC1_42_REF2-
- U1 pad 44: AVSS -> /ADC1_42_REF2-
- U1 pad 5: AVSS -> /ADC1_42_REF2-
- U1 pad 50: AVSS -> /ADC1_42_REF2-
- U1 pad 53: AVSS -> /ADC1_42_REF2-
- U1 pad 60: AVSS -> /ADC1_42_REF2-
- U1 pad 61: AVSS -> /ADC1_42_REF2-
- U1 pad 65: AVSS -> /ADC1_42_REF2-
- U1 pad 7: AVSS -> /ADC1_42_REF2-
- U13 pad 1: /SD/1 -> /SD/1_DATA2
- U13 pad 2: /SD/2 -> /SD/2_DATA3
- U13 pad 3: /SD/3 -> /SD/3_CMD
- U13 pad 4: /SD/4 -> /SD/4_VDD
- U13 pad 5: /SD/5 -> /SD/5_CLK
- U13 pad 6: /SD/6 -> /SD/6_Vss
- U13 pad 7: /SD/7 -> /SD/7_DATA0
- U13 pad 8: /SD/8 -> /SD/8_DATA1
- U13 pad 9: /SD/9 -> /SD/9_DETECT
- U2 pad 22: DGND -> /ADC2_22_DGND
- U2 pad 42: AVSS -> /ADC2_42_REF2-
- U2 pad 44: AVSS -> /ADC2_42_REF2-
- U2 pad 5: AVSS -> /ADC2_42_REF2-
- U2 pad 50: AVSS -> /ADC2_42_REF2-
- U2 pad 53: AVSS -> /ADC2_42_REF2-
- U2 pad 60: AVSS -> /ADC2_42_REF2-
- U2 pad 61: AVSS -> /ADC2_42_REF2-
- U2 pad 65: AVSS -> /ADC2_42_REF2-
- U2 pad 7: AVSS -> /ADC2_42_REF2-
- U3 pad 22: DGND -> /ADC3_22_DGND
- U3 pad 42: AVSS -> /ADC3_42_REF2-
- U3 pad 44: AVSS -> /ADC3_42_REF2-
- U3 pad 5: AVSS -> /ADC3_42_REF2-
- U3 pad 50: AVSS -> /ADC3_42_REF2-
- U3 pad 53: AVSS -> /ADC3_42_REF2-
- U3 pad 60: AVSS -> /ADC3_42_REF2-
- U3 pad 61: AVSS -> /ADC3_42_REF2-
- U3 pad 65: AVSS -> /ADC3_42_REF2-
- U3 pad 7: AVSS -> /ADC3_42_REF2-
- U4 pad 22: DGND -> /ADC4_22_DGND
- U4 pad 42: AVSS -> /ADC4_42_REF2-
- U4 pad 44: AVSS -> /ADC4_42_REF2-
- U4 pad 5: AVSS -> /ADC4_42_REF2-
- U4 pad 50: AVSS -> /ADC4_42_REF2-
- U4 pad 53: AVSS -> /ADC4_42_REF2-
- U4 pad 60: AVSS -> /ADC4_42_REF2-
- U4 pad 61: AVSS -> /ADC4_42_REF2-
- U4 pad 65: AVSS -> /ADC4_42_REF2-
- U4 pad 7: AVSS -> /ADC4_42_REF2-
- U8 pad 1: /CRYSTAL/1 -> /CRYSTAL/1_NC
- U8 pad 2: /CRYSTAL/2 -> /CRYSTAL_2_GND
- U8 pad 3: /CRYSTAL/3 -> /CRYSTAL_3_OUT
- U8 pad 4: /CRYSTAL/4 -> /CRYSTAL_4_Vin
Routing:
- net AVSS: track 457.7 -> 0.00 mm
- net /ADC3_42_REF2-: track 0.00 -> 114.4 mm
- net /ADC4_42_REF2-: track 0.00 -> 114.4 mm
- net /ADC1_42_REF2-: track 0.00 -> 114.4 mm
- net /ADC2_42_REF2-: track 0.00 -> 114.4 mm
- net DGND: track 36.1 -> 0.00 mm
- net /MCU_107_VSS: track 206.9 -> 236.9 mm, vias 0 -> 11
- net /SD/8_DATA1: track 0.00 -> 18.4 mm
- net /USB/6_Shield: track 0.00 -> 17.9 mm
- net /SD/4_VDD: track 0.00 -> 17.7 mm
- net /SD/6_Vss: track 0.00 -> 17.3 mm
- net /SD/2_DATA3: track 0.00 -> 17.0 mm
- net /SD/5: track 16.1 -> 0.00 mm
- net /SD/1_DATA2: track 0.00 -> 14.8 mm
- net /SD/4: track 14.3 -> 0.00 mm
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- added copper zone on B.Cu, net /ACCEL&GYRO/6_GND
- added copper zone on B.Cu, net /ADC1_22_DGND
- added copper zone on B.Cu, net /ADC1_42_REF2-
- added copper zone on B.Cu, net /ADC2_22_DGND
- added copper zone on B.Cu, net /ADC2_42_REF2-
- added copper zone on B.Cu, net /ADC3_22_DGND
- added copper zone on B.Cu, net /ADC3_42_REF2-
- added copper zone on B.Cu, net /ADC4_22_DGND
- added copper zone on B.Cu, net /ADC4_42_REF2-
- added copper zone on B.Cu, net /AVDD_2_GND
- added copper zone on B.Cu, net /CRYSTAL_2_GND
- added copper zone on B.Cu, net /IOVDD_2_GND
- added copper zone on B.Cu, net /REF_4_GND
- added copper zone on B.Cu, net /SD/6_Vss
- added copper zone on B.Cu, net /VDD_2_GND
- removed copper zone on B.Cu, net AVSS
- removed copper zone on B.Cu, net DGND
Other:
- outline, holes or cut-outs redrawn
